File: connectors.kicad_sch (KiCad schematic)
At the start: 4 parts, among them J1 Conn_01x04_Pin, J2 Conn_01x04_Pin, J3 Conn_01x09_Pin, J4 Conn_02x03_Odd_Even

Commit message: footprints
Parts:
- J1, J2: footprint (none) -> Connector_PinHeader_2.54mm:PinHeader_1x04_P2.54mm_Vertical
- J3: footprint (none) -> Connector_PinHeader_2.54mm:PinHeader_1x09_P2.54mm_Vertical
- J4: footprint (none) -> Connector_PinHeader_2.54mm:PinHeader_2x03_P2.54mm_Vertical
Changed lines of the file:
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@@
 			)
 		)
-		(property "Footprint" ""
+		(property "Footprint" "Connector_PinHeader_2.54mm:PinHeader_2x03_P2.54mm_Vertical"
 			(at 93.98 85.09 0)
 			(effects
@@
 			)
 		)
-		(property "Footprint" ""
+		(property "Footprint" "Connector_PinHeader_2.54mm:PinHeader_1x04_P2.54mm_Vertical"
 			(at 97.79 67.31 0)
 			(effects
@@
 			)
 		)
-		(property "Footprint" ""
+		(property "Footprint" "Connector_PinHeader_2.54mm:PinHeader_1x04_P2.54mm_Vertical"
 			(at 72.39 67.31 0)
 			(effects
@@
 			)
 		)
-		(property "Footprint" ""
+		(property "Footprint" "Connector_PinHeader_2.54mm:PinHeader_1x09_P2.54mm_Vertical"
 			(at 119.38 74.93 0)
 			(effects

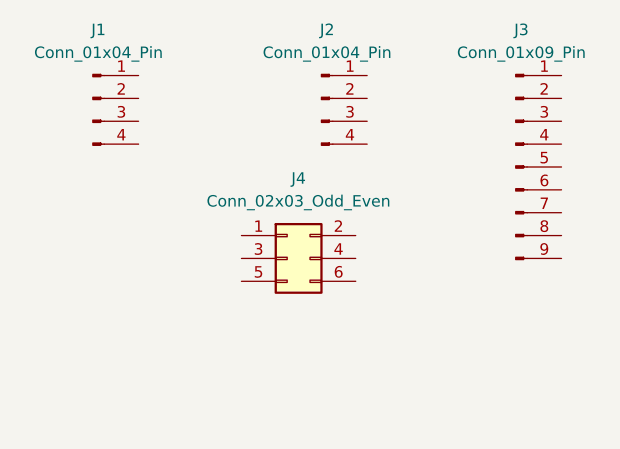
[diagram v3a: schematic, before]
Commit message: schematic wiring
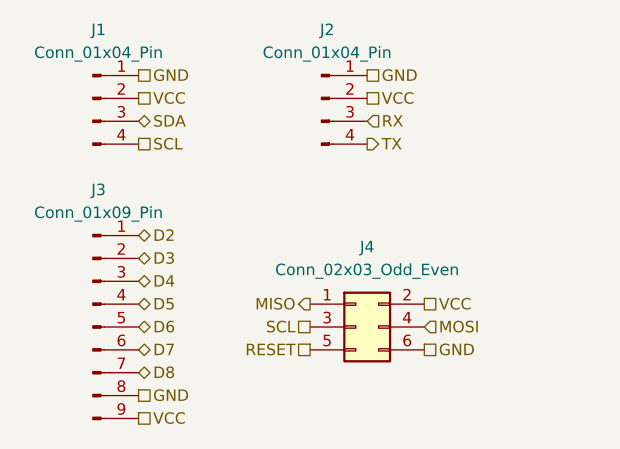
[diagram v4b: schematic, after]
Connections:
- net MISO: now reaches J4.1 (Pin_1)
- net VCC: now reaches J4.2 (Pin_2)
- net VCC: now also J1.2 (Pin_2), J2.2 (Pin_2), J3.9 (Pin_9)
- net SCL: now reaches J4.3 (Pin_3)
- net SCL: now also J1.4 (Pin_4)
- net MOSI: now reaches J4.4 (Pin_4)
- net RESET: now reaches J4.5 (Pin_5)
- net GND: now reaches J4.6 (Pin_6)
- net GND: now also J1.1 (Pin_1), J2.1 (Pin_1), J3.8 (Pin_8)
- net RX: now reaches J2.3 (Pin_3)
- net TX: now reaches J2.4 (Pin_4)
- net SDA: now reaches J1.3 (Pin_3)
- net D2: now reaches J3.1 (Pin_1)
- net D3: now reaches J3.2 (Pin_2)
- net D4: now reaches J3.3 (Pin_3)
- net D5: now reaches J3.4 (Pin_4)
- net D6: now reaches J3.5 (Pin_5)
- net D7: now reaches J3.6 (Pin_6)
- net D8: now reaches J3.7 (Pin_7)
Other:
- moved on the sheet: J3, J4
